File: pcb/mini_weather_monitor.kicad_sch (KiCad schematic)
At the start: 10 parts, among them J1 SW-520D, U1 PowerSupplyMB102_v13, U2 4.0inch_SPI_MSP4021, U2_BME280 module_bme280, U3_BH1750 module_bh1750

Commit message: revamping a bit
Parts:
- removed J1: SW-520D, tilt:KY020 Tilt, symbol Connector_Generic:Conn_01x03
- removed U1: PowerSupplyMB102_v13, power_supplies:POWERSUPPLYMB102, symbol power_supplyies:PowerSupplyMB102_v13
- added 5V_buck_boost1: ~, regulator_voltage:S09_HVN, symbol voltage_regulator:S09_HVN
- added USB_C_Input1: ~, custom_usbc:USB_C_breakout_power_only, symbol usb_breakout:USB_C_Breakout
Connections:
- net GND: now also 5V_buck_boost1.1 (VOUT-), 5V_buck_boost1.5 (VIN-), USB_C_Input1.2 (VIN-)
- net VCC: now also 5V_buck_boost1.2 (VOUT+)
- new net: 5V_buck_boost1.3 (EN), 5V_buck_boost1.4 (VIN+), USB_C_Input1.1 (VIN+)

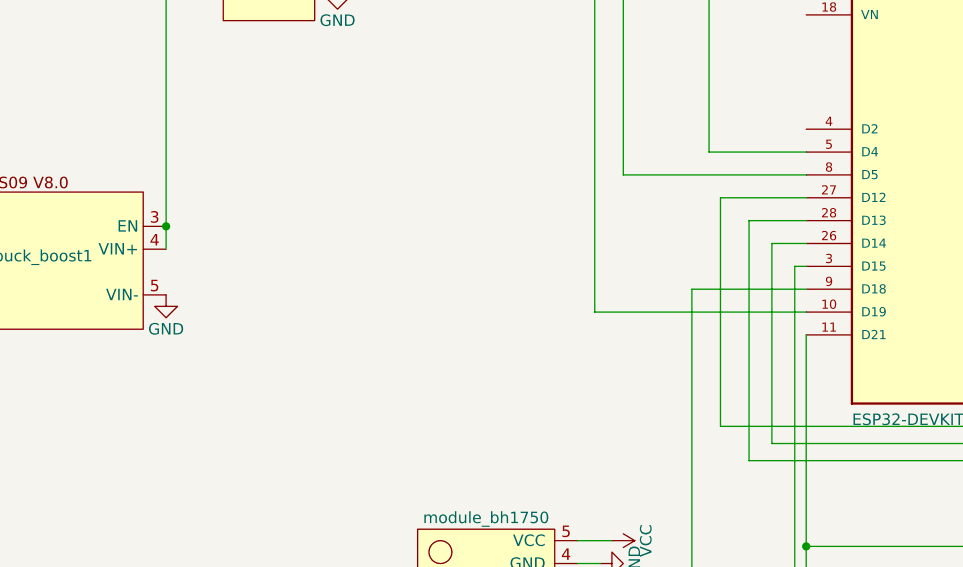
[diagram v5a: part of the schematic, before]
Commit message: adding extra usb input
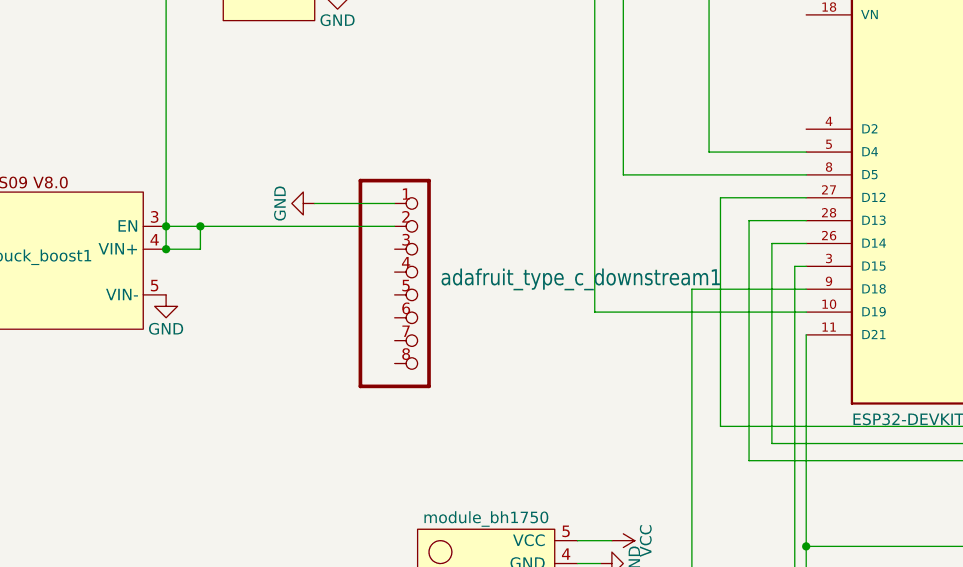
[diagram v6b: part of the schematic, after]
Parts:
- added adafruit_type_c_downstream1: ~, custom_usbc:Adafruit USB Type C Breakout rev B, symbol Adafruit USB Type C Downstream Breakout rev B-eagle-import:HEADER-1X8
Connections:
- net GND: now also adafruit_type_c_downstream1.1
- net at 5V_buck_boost1.3 (EN), 5V_buck_boost1.4 (VIN+), USB_C_Input1.1 (VIN+): now also adafruit_type_c_downstream1.2
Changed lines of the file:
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@@
+	)
+	(junction
+		(at 54.61 82.55)
+		(diameter 0)
+		(color 0 0 0 0)
+	)
+	(junction
+		(at 58.42 80.01)
+		(diameter 0)
+		(color 0 0 0 0)
 	)
 	(junction
@@
 	(wire
 		(pts
+			(xy 58.42 80.01) (xy 80.01 80.01)
+		)
+		(stroke
+			(width 0)
+			(type default)
+		)
+	)
+	(wire
+		(pts
 			(xy 184.785 104.14) (xy 121.92 104.14)
 		)
@@
 	(wire
 		(pts
+			(xy 71.12 77.47) (xy 80.01 77.47)
+		)
+		(stroke
+			(width 0)
+			(type default)
+		)
+	)
+	(wire
+		(pts
 			(xy 194.31 107.315) (xy 194.31 115.57)
 		)
@@
 	(wire
 		(pts
+			(xy 58.42 80.01) (xy 58.42 82.55)
+		)
+		(stroke
+			(width 0)
+			(type default)
+		)
+	)
+	(wire
+		(pts
 			(xy 205.105 73.025) (xy 182.88 73.025)
 		)
@@
 	(wire
 		(pts
+			(xy 54.61 82.55) (xy 58.42 82.55)
+		)
+		(stroke
+			(width 0)
+			(type default)
+		)
+	)
+	(wire
+		(pts
 			(xy 156.21 46.355) (xy 158.75 46.355)
 		)
@@
 		(pts
 			(xy 125.73 115.57) (xy 125.73 122.555)
+		)
+		(stroke
+			(width 0)
+			(type default)
+		)
+	)
+	(wire
+		(pts
+			(xy 54.61 80.01) (xy 58.42 80.01)
 		)
 		(stroke
@@
 	)
 	(symbol
+		(lib_id "power:GND")
+		(at 71.12 77.47 270)
+		(unit 1)
+		(exclude_from_sim no)
+		(in_bom yes)
+		(on_board yes)
+		(dnp no)
+		(property "Reference" "#PWR05"
+			(at 64.77 77.47 0)
+			(effects
+				(font
+					(size 1.27 1.27)
+				)
+				(hide yes)
+			)
+		)
+		(property "Value" "GND"
+			(at 67.31 77.47 0)
+			(effects
+				(font
+					(size 1.27 1.27)
+				)
+			)
+		)
+		(property "Footprint" ""
+			(at 71.12 77.47 0)
+			(effects
+				(font
+					(size 1.27 1.27)
+				)
+				(hide yes)
+			)
+		)
+		(property "Datasheet" ""
+			(at 71.12 77.47 0)
+			(effects
+				(font
+					(size 1.27 1.27)
+				)
+				(hide yes)
+			)
+		)
+		(property "Description" ""
+			(at 71.12 77.47 0)
+			(effects
+				(font
+					(size 1.27 1.27)
+				)
+				(hide yes)
+			)
+		)
+		(pin "1"
+		)
+		(instances
+			(project "mini_weather_monitor"
+				(path "/e63e39d7-6ac0-4ffd-8aa3-1841a4541b55"
+					(reference "#PWR05")
+					(unit 1)
+				)
+			)
+		)
+	)
+	(symbol
 		(lib_id "usini_sensors:module_bh1750")
 		(at 100.33 117.475 180)
@@
 					(unit 1)
 				)
+			)
+		)
+	)
+	(symbol
+		(lib_id "Adafruit USB Type C Downstream Breakout rev B-eagle-import:HEADER-1X8")
+		(at 82.55 87.63 0)
+		(unit 1)
+		(exclude_from_sim no)
+		(in_bom yes)
+		(on_board yes)
+		(dnp no)
+		(fields_autoplaced yes)
+		(property "Reference" "adafruit_type_c_downstream1"
+			(at 85.09 85.725 0)
+			(effects
+				(font
+					(size 1.778 1.5113)
+				)
+				(justify left)
+			)
+		)
+		(property "Value" "~"
+			(at 85.09 88.265 0)
+			(effects
+				(font
+					(size 1.778 1.5113)
+				)
+				(justify left)
+			)
+		)
+		(property "Footprint" "custom_usbc:Adafruit USB Type C Breakout rev B"
+			(at 82.55 87.63 0)
+			(effects
+				(font
+					(size 1.27 1.27)
+				)
+				(hide yes)
+			)
+		)
+		(property "Datasheet" ""
+			(at 82.55 87.63 0)
+			(effects
+				(font
+					(size 1.27 1.27)
+				)
+				(hide yes)
+			)
+		)
+		(property "Description" "PIN HEADER"
+			(at 82.55 87.63 0)
+			(effects
+				(font
+					(size 1.27 1.27)
+				)
+				(hide yes)
+			)
+		)
+		(pin "5"
+		)
+		(pin "6"
+		)
+		(pin "7"
+		)
+		(pin "1"
+		)
+		(pin "8"
+		)
+		(pin "2"
+		)
+		(pin "3"
+		)
+		(pin "4"
+		)
+		(instances
+			(project "mini_weather_monitor"
+				(path "/e63e39d7-6ac0-4ffd-8aa3-1841a4541b55"
+					(reference "adafruit_type_c_downstream1")
+					(unit 1)
+				)

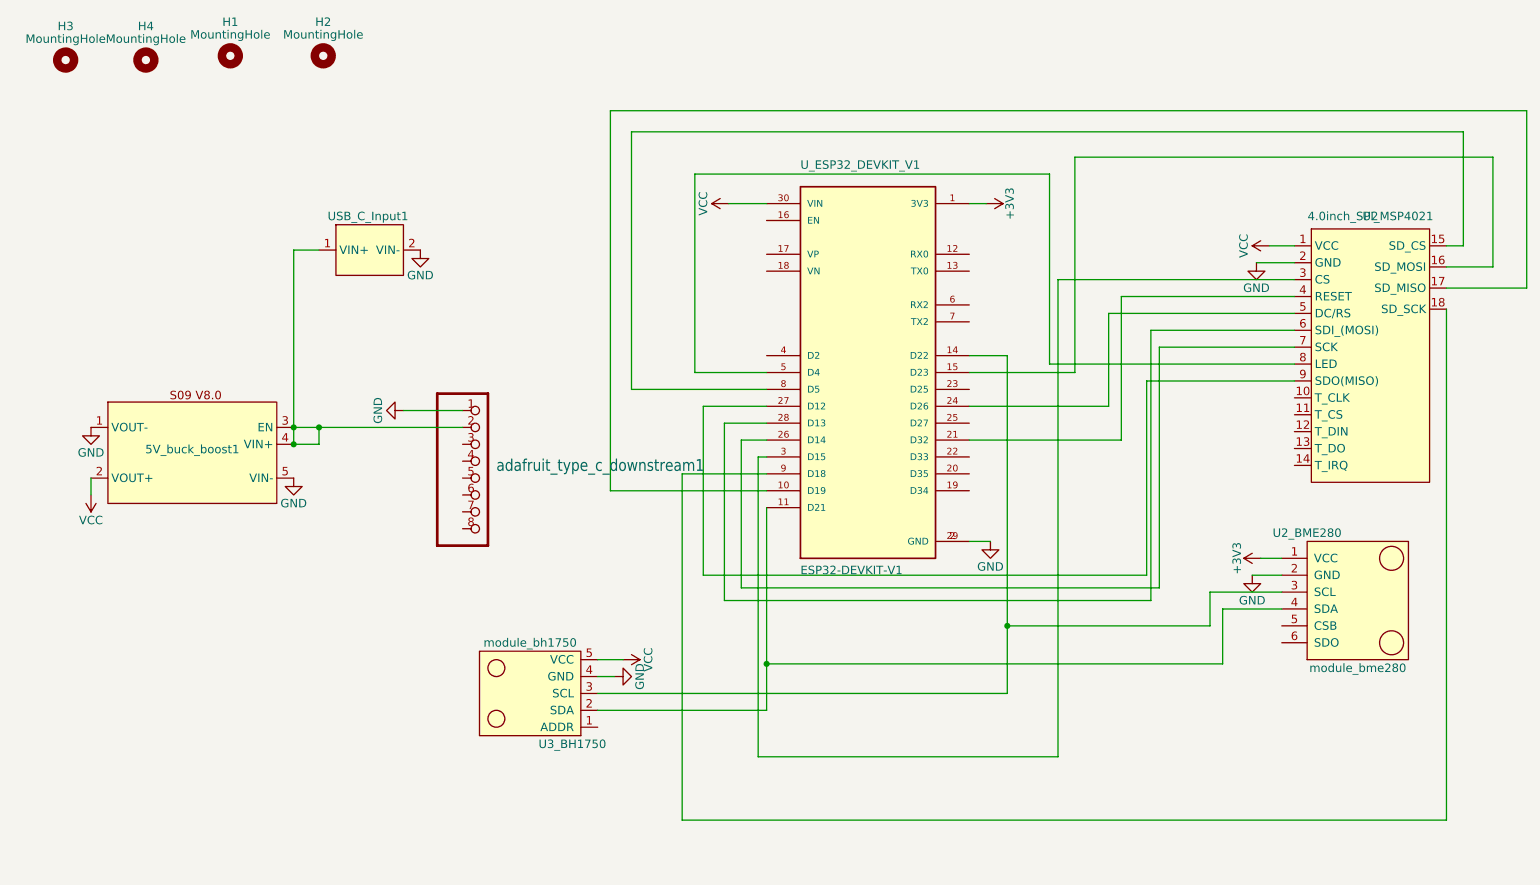
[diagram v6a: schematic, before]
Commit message: using adafruit stuff
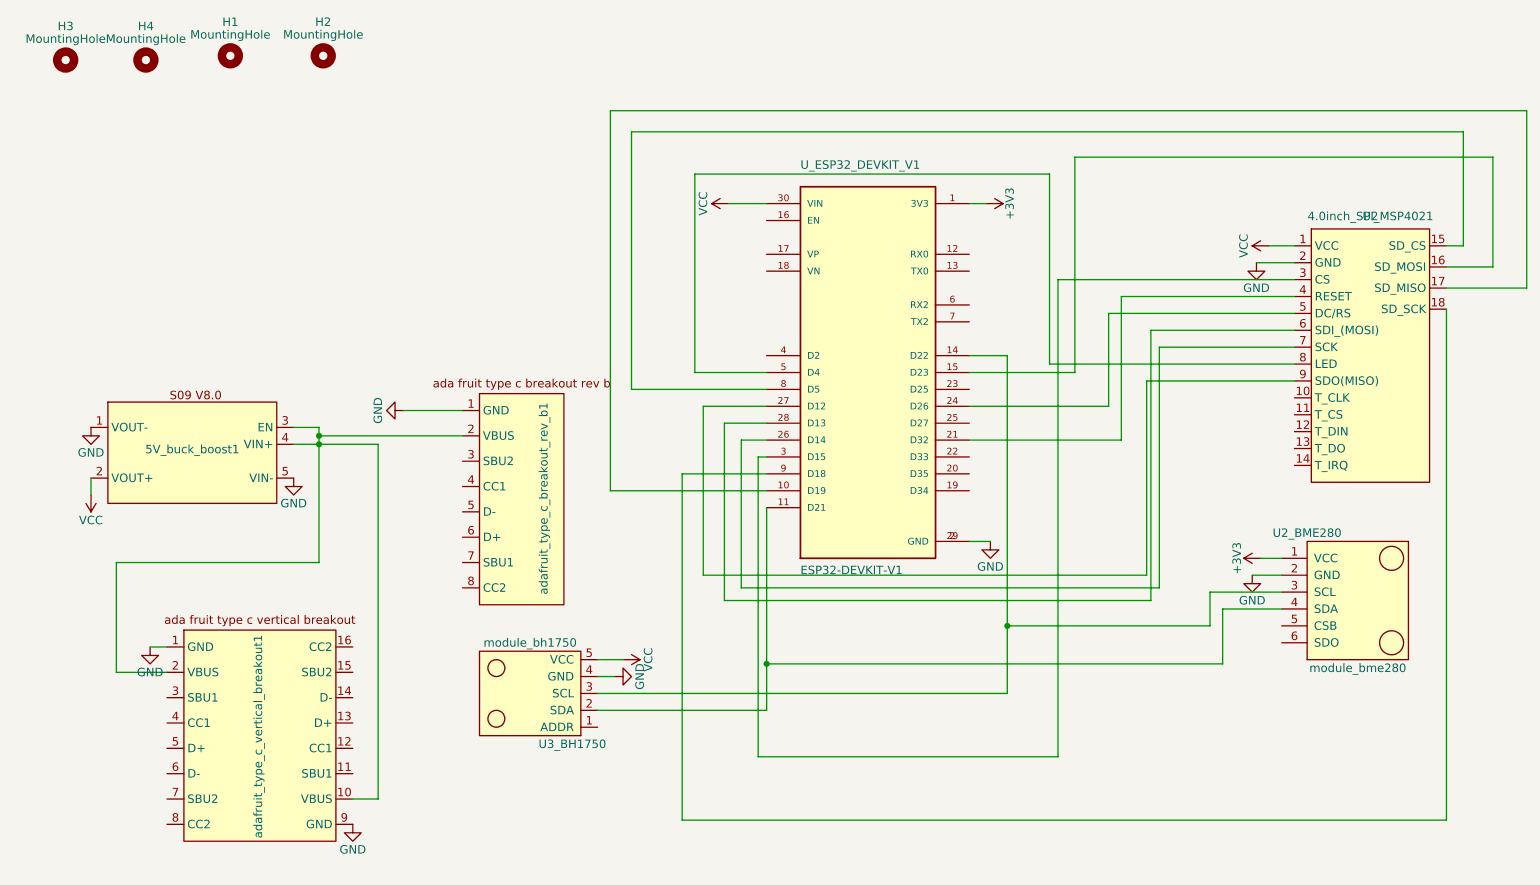
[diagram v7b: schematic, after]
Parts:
- removed USB_C_Input1: ~, custom_usbc:USB_C_breakout_power_only, symbol usb_breakout:USB_C_Breakout
- removed adafruit_type_c_downstream1: ~, custom_usbc:Adafruit USB Type C Breakout rev B, symbol Adafruit USB Type C Downstream Breakout rev B-eagle-import:HEADER-1X8
- added adafruit_type_c_breakout_rev_b1: ~, custom_usbc:Adafruit_USB_Type_C_Breakout_rev_B, symbol usb_breakout:adafruit_usb_type_c_breakout_rev_b
- added adafruit_type_c_vertical_breakout1: ~, custom_usbc:Adafruit_USB_Type_C_Vertical_Breakout, symbol usb_breakout:adafruit_usb_type_c_vertical_breakout
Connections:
- net GND: now also adafruit_type_c_breakout_rev_b1.1 (GND), adafruit_type_c_vertical_breakout1.1 (GND), adafruit_type_c_vertical_breakout1.9 (GND)
- net at 5V_buck_boost1.3 (EN), 5V_buck_boost1.4 (VIN+): now also adafruit_type_c_breakout_rev_b1.2 (VBUS), adafruit_type_c_vertical_breakout1.10 (VBUS), adafruit_type_c_vertical_breakout1.2 (VBUS)

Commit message: adding caps and diodes
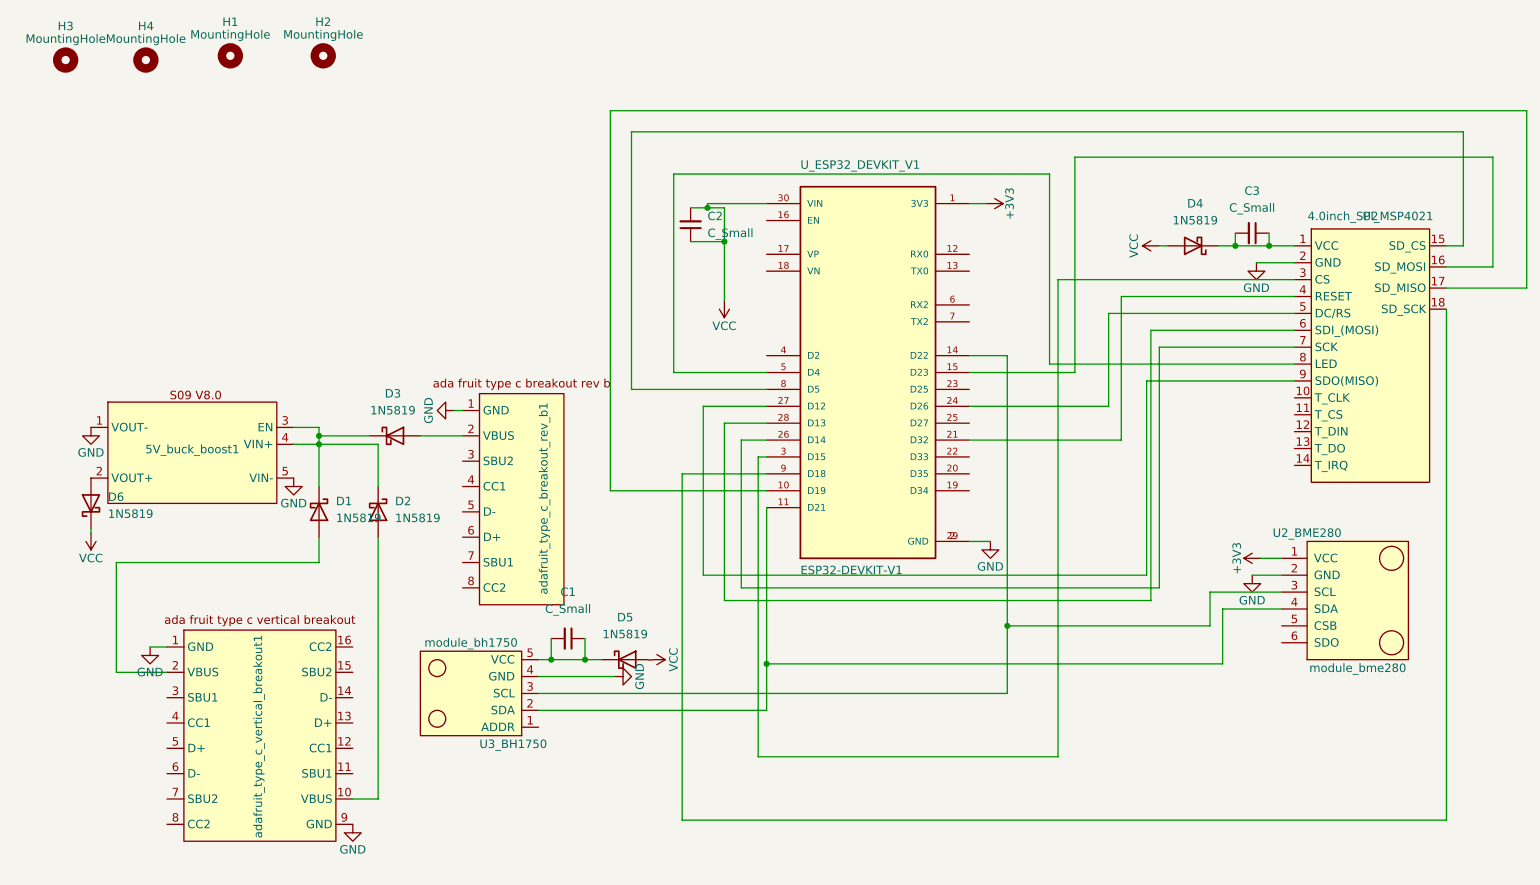
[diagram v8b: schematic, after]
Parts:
- added C1, C2, C3: C_Small, Capacitor_SMD:C_1206_3216Metric_Pad1.33x1.80mm_HandSolder, symbol Device:C_Small
- added D1, D2, D3, D4, D5, D6: 1N5819, Diode_SMD:D_SOD-123, symbol Diode:1N5819
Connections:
- net VCC: now also C2.1, C2.2, D4.2 (A), D5.2 (A), D6.1 (K); no longer 5V_buck_boost1.2 (VOUT+), U2.1 (VCC), U3_BH1750.5 (VCC)
- new net: C3.1, C3.2, D4.1 (K), U2.1 (VCC)
- new net: 5V_buck_boost1.2 (VOUT+), D6.2 (A)
- new net: 5V_buck_boost1.3 (EN), 5V_buck_boost1.4 (VIN+), D1.1 (K), D2.1 (K), D3.1 (K)
- new net: C1.1, C1.2, D5.1 (K), U3_BH1750.5 (VCC)
- new net: D3.2 (A), adafruit_type_c_breakout_rev_b1.2 (VBUS)
- new net: D1.2 (A), adafruit_type_c_vertical_breakout1.2 (VBUS)
- new net: D2.2 (A), adafruit_type_c_vertical_breakout1.10 (VBUS)
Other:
- moved on the sheet: U3_BH1750
